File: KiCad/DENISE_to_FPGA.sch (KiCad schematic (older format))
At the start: 15 parts, among them J1 Conn_01x02, J2 Conn_01x02, J3 Conn_01x40, U1 LM1117-3.3, U2 74LVC245A, U3 74LVC245A, U4 74LVC1G86, U5 Denise_MB_PinHeader

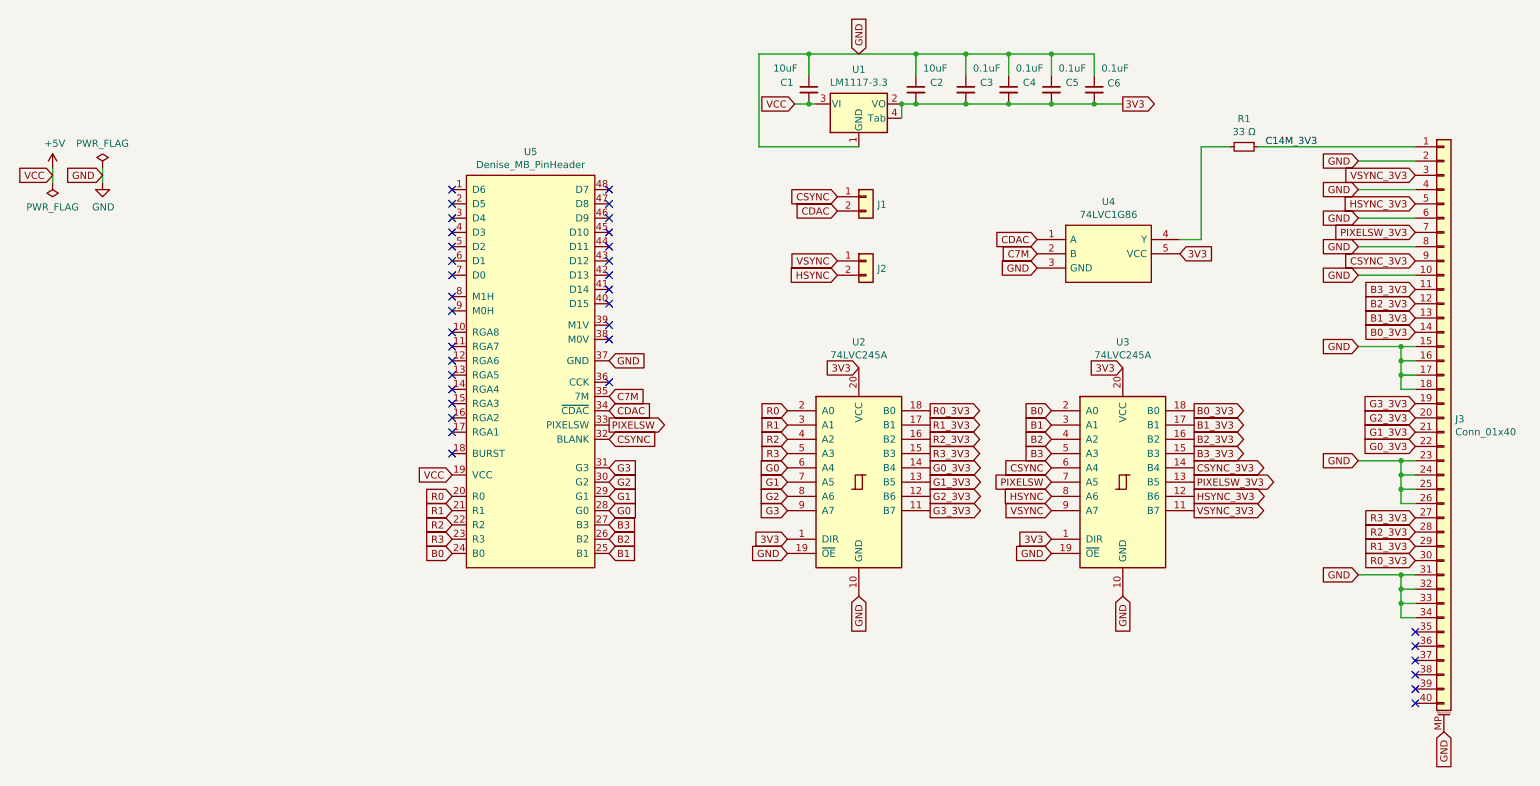
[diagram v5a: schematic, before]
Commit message: Updated design with a 74LVC162244ADGG, changed PCB size and TH-pins
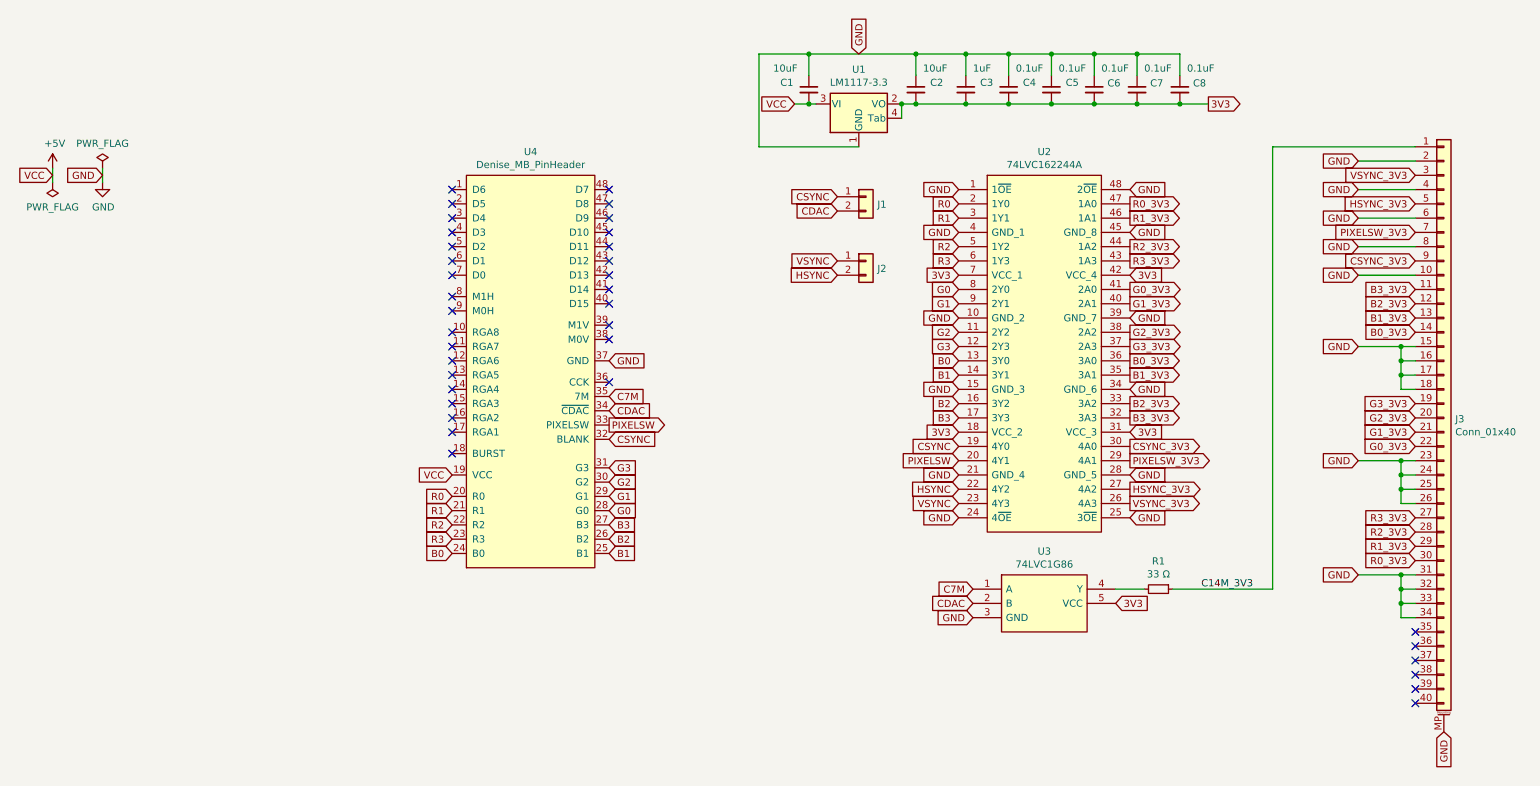
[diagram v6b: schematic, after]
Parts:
- removed U2, U3: 74LVC245A, Package_SO:TSSOP-20_4.4x6.5mm_P0.65mm, symbol DENISE_to_FPGA:74LVC245A
- removed U4: 74LVC1G86, Package_TO_SOT_SMD:SOT-353_SC-70-5_Handsoldering, symbol DENISE_to_FPGA:74LVC1G86
- added C7, C8: 0.1uF, DENISE_to_FPGA:C_0805_2012Metric_Pad1.15x1.4mm_HandSolder, symbol Device:C_Small
- added U2: 74LVC162244A, Package_SO:TSSOP-48_6.1x12.5mm_P0.5mm, symbol DENISE_to_FPGA:74LVC162244A
- added U3: 74LVC1G86, Package_TO_SOT_SMD:SOT-353_SC-70-5_Handsoldering, symbol DENISE_to_FPGA:74LVC1G86
- C3: value 0.1uF -> 1uF
- C4, C5: footprint Capacitor_SMD:C_0805_2012Metric_Pad1.15x1.40mm_HandSolder -> DENISE_to_FPGA:C_0805_2012Metric_Pad1.15x1.4mm_HandSolder
- C6: footprint Capacitor_SMD:C_0805_2012Metric_Pad1.18x1.45mm_HandSolder -> DENISE_to_FPGA:C_0805_2012Metric_Pad1.15x1.4mm_HandSolder
- renumbered U5 to U4
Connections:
- net 3V3: now also C7.2, C8.2, U2.18 (VCC_2), U2.31 (VCC_3), U2.42 (VCC_4), U2.7 (VCC_1), U3.5 (VCC)
- net B0: now also U2.13 (3Y0)
- net B0_3V3: now also U2.36 (3A0)
- net B1: now also U2.14 (3Y1)
- net B1_3V3: now also U2.35 (3A1)
- net B2: now also U2.16 (3Y2)
- net B2_3V3: now also U2.33 (3A2)
- net B3: now also U2.17 (3Y3)
- net B3_3V3: now also U2.32 (3A3)
- net C7M: now also U3.1 (A)
- net CDAC: now also U3.2 (B)
- net CSYNC: now also U2.19 (4Y0)
- net CSYNC_3V3: now also U2.30 (4A0)
- net G0: now also U2.8 (2Y0)
- net G0_3V3: now also U2.41 (2A0)
- net G1: now also U2.9 (2Y1)
- net G1_3V3: now also U2.40 (2A1)
- net G2: now also U2.11 (2Y2)
- net G2_3V3: now also U2.38 (2A2)
- net G3: now also U2.12 (2Y3)
- net G3_3V3: now also U2.37 (2A3)
- net GND: now also C7.1, C8.1, U2.1 (1~OE), U2.10 (GND_2), U2.15 (GND_3), U2.21 (GND_4), U2.24 (4~OE), U2.25 (3~OE), U2.28 (GND_5), U2.34 (GND_6), U2.39 (GND_7), U2.4 (GND_1), U2.45 (GND_8), U2.48 (2~OE), U3.3 (GND)
- net HSYNC: now also U2.22 (4Y2)
- net HSYNC_3V3: now also U2.27 (4A2)
- net PIXELSW: now also U2.20 (4Y1)
- net PIXELSW_3V3: now also U2.29 (4A1)
- net R0: now also U2.2 (1Y0)
- net R0_3V3: now also U2.47 (1A0)
- net R1: now also U2.3 (1Y1)
- net R1_3V3: now also U2.46 (1A1)
- net R2: now also U2.5 (1Y2)
- net R2_3V3: now also U2.44 (1A2)
- net R3: now also U2.6 (1Y3)
- net R3_3V3: now also U2.43 (1A3)
- net VSYNC: now also U2.23 (4Y3)
- net VSYNC_3V3: now also U2.26 (4A3)
- net at R1.2: now also U3.4 (Y)
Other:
- moved on the sheet: R1

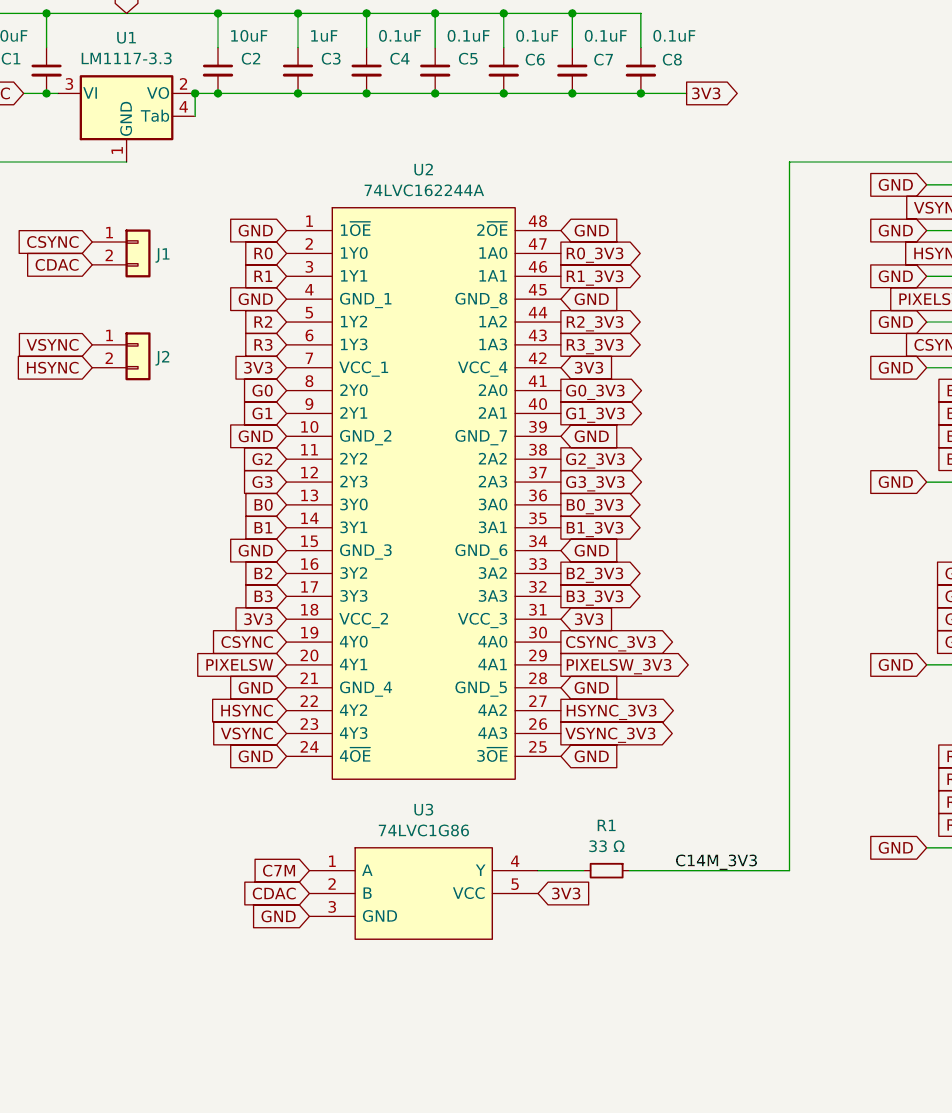
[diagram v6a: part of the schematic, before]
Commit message: changed U3 from 74LVC1G86 (XOR-gate, TSSOP-5) to 74LVC1G57GV (XNOR-gate, TSOP-6)
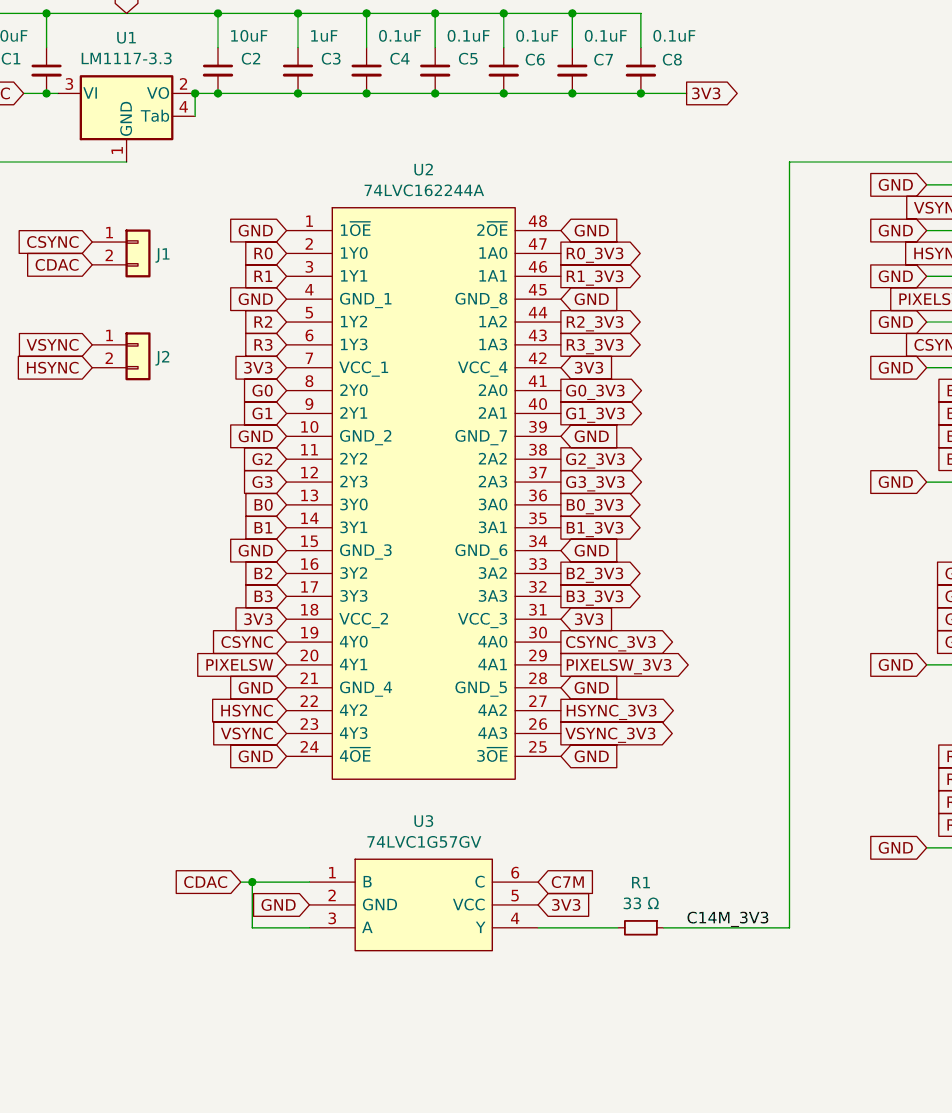
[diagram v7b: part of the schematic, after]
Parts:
- removed U3: 74LVC1G86, Package_TO_SOT_SMD:SOT-353_SC-70-5_Handsoldering, symbol DENISE_to_FPGA:74LVC1G86
- added U3: 74LVC1G57GV, Package_SO:TSOP-6_1.65x3.05mm_P0.95mm, symbol DENISE_to_FPGA:74LVC1G57GV
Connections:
- net 3V3: now also U3.5 (VCC)
- net C7M: now also U3.6 (C)
- net CDAC: now also U3.1 (B), U3.3 (A)
- net GND: now also U3.2 (GND)
- net at R1.2: now also U3.4 (Y)
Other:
- moved on the sheet: R1
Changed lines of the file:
@@
 L Device:R_Small R1
 U 1 1 64FE39F6
-P 8650 4600
-F 0 "R1" V 8454 4600 50  0000 C CNN
-F 1 "33 Ω" V 8545 4600 50  0000 C CNN
-F 2 "Resistor_SMD:R_0805_2012Metric_Pad1.20x1.40mm_HandSolder" H 8650 4600 50  0001 C CNN
-F 3 "~" H 8650 4600 50  0001 C CNN
-	1    8650 4600
+P 8800 4850
+F 0 "R1" V 8604 4850 50  0000 C CNN
+F 1 "33 Ω" V 8695 4850 50  0000 C CNN
+F 2 "Resistor_SMD:R_0805_2012Metric_Pad1.20x1.40mm_HandSolder" H 8800 4850 50  0001 C CNN
+F 3 "~" H 8800 4850 50  0001 C CNN
+	1    8800 4850
 	0    1    1    0
 $EndComp
-Wire Wire Line
-	8350 4600 8550 4600
-Text Label 8950 4600 0    50   ~ 0
+Text Label 9000 4850 0    50   ~ 0
 C14M_3V3
 NoConn ~ 10450 5400
@@
 	9000 1200 8800 1200
 Connection ~ 8800 1200
-$Comp
-L DENISE_to_FPGA:74LVC1G86 U3
-U 1 1 66FC0049
-P 7850 4700
-F 0 "U3" H 7850 5065 50  0000 C CNN
-F 1 "74LVC1G86" H 7850 4974 50  0000 C CNN
-F 2 "Package_TO_SOT_SMD:SOT-353_SC-70-5_Handsoldering" H 8200 4900 50  0001 L CNN
-F 3 "" H 8200 4800 50  0001 L CNN
-	1    7850 4700
-	1    0    0    -1
-$EndComp
-Text GLabel 8350 4700 2    50   Input ~ 0
+Text GLabel 8350 4750 2    50   Input ~ 0
 3V3
-Text GLabel 7350 4700 0    50   Input ~ 0
+Text GLabel 7050 4650 0    50   Input ~ 0
 CDAC
-Text GLabel 7350 4800 0    50   Input ~ 0
-GND
-Wire Wire Line
-	8750 4600 9450 4600
-Wire Wire Line
-	9450 4600 9450 1500
+Text GLabel 7350 4750 0    50   Input ~ 0
+GND
 Wire Wire Line
 	9450 1500 10450 1500
-Text GLabel 7350 4600 0    50   Input ~ 0
+Text GLabel 8350 4650 2    50   Input ~ 0
 C7M
+$Comp
+L DENISE_to_FPGA:74LVC1G57GV U3
+U 1 1 66FF807E
+P 7850 4750
+F 0 "U3" H 7850 5115 50  0000 C CNN
+F 1 "74LVC1G57GV" H 7850 5024 50  0000 C CNN
+F 2 "Package_SO:TSOP-6_1.65x3.05mm_P0.95mm" H 8200 4950 50  0001 L CNN
+F 3 "" H 8200 4850 50  0001 L CNN
+	1    7850 4750
+	1    0    0    -1
+$EndComp
+Wire Wire Line
+	9450 1500 9450 4850
+Wire Wire Line
+	8900 4850 9450 4850
+Wire Wire Line
+	8350 4850 8700 4850
+Wire Wire Line
+	7050 4650 7100 4650
+Wire Wire Line
+	7100 4650 7100 4850
+Wire Wire Line
+	7100 4850 7350 4850
+Connection ~ 7100 4650
+Wire Wire Line
+	7100 4650 7350 4650
 $EndSCHEMATC
